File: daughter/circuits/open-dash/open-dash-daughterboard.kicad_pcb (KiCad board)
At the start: 4 copper layers, 125 x 100.1 mm, 220 parts, among them J1 Conn_01x01_Female, J10 Barrel_Jack_OD5.5_ID2.5, J11 Barrel_Jack_OD5.5_ID2.5, J12 AudioJack_3.5TRS, J13 AudioJack_3.5TRS, J14 Conn_02x03_Odd_Even, J15 USB_MINI_B, J16 Conn_02x02_Counter_Clockwise, J2 Conn_01x01_Female, J3 Conn_01x01_Female, J4 Conn_01x01_Female, J42 Conn_02x02_Counter_Clockwise, J43 Conn_02x02_Counter_Clockwise, J5 Conn_02x06_Odd_Even, J6 Conn_IDE_40, J7 Conn_IDE_40, J8 Conn_IDE_40, J9 Barrel_Jack_OD5.5_ID2.5, Q1 Crystal_12Mhz, Q10 Q_NPN_BEC, Q11 Q_AO3401A, Q12 Q_NPN_BEC, Q13 Q_NPN_BEC, Q14 Q_AO3400A, Q15 Q_NPN_BEC, Q16 Q_NPN_BEC, Q17 Q_AO3401A, Q18 Q_NPN_BEC, Q19 Q_NPN_BEC, Q2 Q_SS8050, Q20 Q_AO3400A, Q21 Q_NPN_BEC, Q22 Q_NPN_BEC, Q23 Q_AO3401A, Q24 Q_AO3400A, Q25 Q_AO3401A, Q26 Q_AO3400A, Q27 Q_AO3401A, Q28 Q_AO3400A, Q29 Q_AO3401A, Q3 Q_NPN_BEC, Q30 Q_AO3400A, Q31 Q_AO3401A, Q32 Q_AO3400A, Q33 Q_AO3401A, Q34 Q_AO3400A, Q35 Q_AO3401A, Q36 Q_AO3400A, Q37 Q_AO3401A, Q38 Q_AO3400A, Q39 Q_SS8550, Q4 Q_NPN_BEC, Q40 Q_AO3401A, Q5 Q_NPN_BEC, Q6 Q_NPN_BEC, Q7 Q_NPN_BEC, Q8 Q_NPN_BEC, Q9 Q_NPN_BEC, T1 Audio_Transformer, T2 Audio_Transformer, T3 Audio_Transformer, T4 Audio_Transformer, U1 Opto_TLP521, U10 Temp_Hum_HDC1080DMBR, U11 REG_AMS1117-3.3, U12 CH340T(SSOP20W), U13 MCP23017_SS, U14 ADC_ADS1015, U15 ADC_ADS1015, U16 ADC_ADS1015, U2 ACS711, U3 CAN_MCP2551-I-SN, U4 MIC29302WU, U5 MIC29302WU, U6 MIC29302WU, U7 TDA7851F, U8 Opto_TLP521, U9 ESP32-WROOM-32

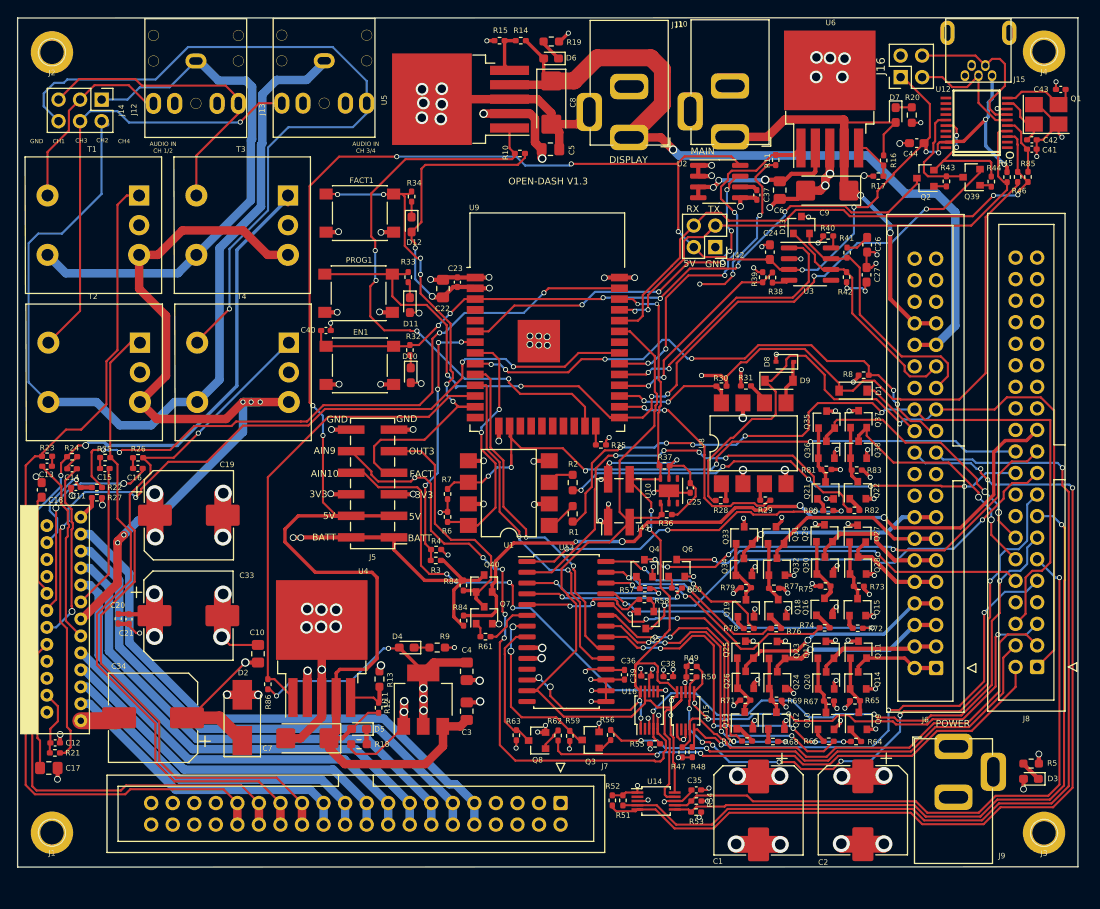
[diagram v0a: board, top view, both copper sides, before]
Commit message: send v1.4 to board house. Corrected source-drain on fets.
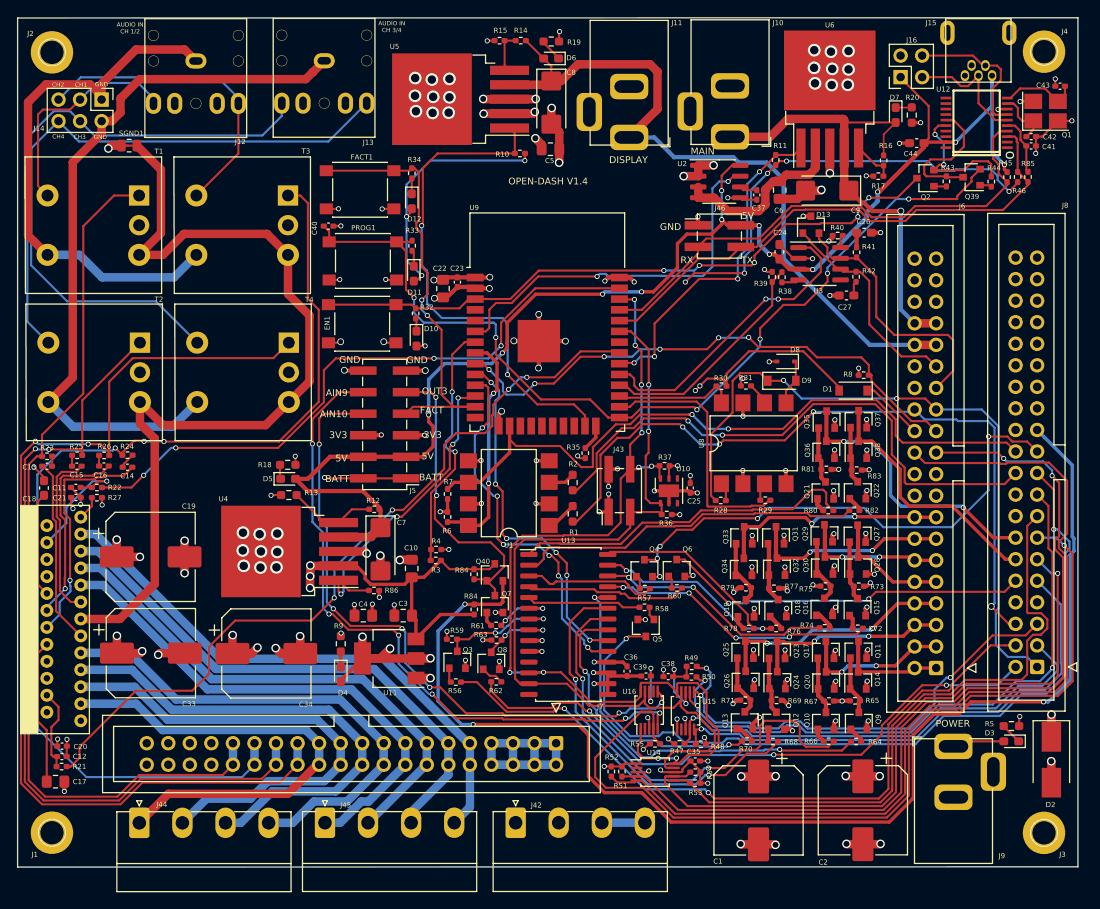
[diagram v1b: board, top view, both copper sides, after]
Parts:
- added J44: Terminal_01x04, Open_Automation:Terminal_1,5_4-G-5.08_1x04_P5.08mm_Horizontal, F.Cu at (102.5, 135.7)
- added J45: Terminal_01x04, Open_Automation:Terminal_1,5_4-G-5.08_1x04_P5.08mm_Horizontal, F.Cu at (124.4, 135.7)
- added J46: Conn_02x02_Counter_Clockwise, Connector_PinHeader_2.54mm:PinHeader_2x02_P2.54mm_Vertical_SMD, F.Cu at (170.9, 66.5)
- added SGND1: SGND_CONN, Open_Automation:SGND_CONN, F.Cu at (101.3, 55.9)
- D1, D9: value D_1N5819HW -> D_B5819W
- J42: value Conn_02x02_Counter_Clockwise -> Terminal_01x04; footprint Connector_PinHeader_2.54mm:PinHeader_2x02_P2.54mm_Vertical -> Open_Automation:Terminal_1,5_4-G-5.08_1x04_P5.08mm_Horizontal
- moved D2 95.5 mm to (210.0, 128.3), turned to 270 degrees
- moved J42 71.8 mm to (146.9, 135.7), turned to 0 degrees
- moved R18 34.0 mm to (120.0, 93.5), turned to 0 degrees
- moved D5 30.7 mm to (120.0, 95.2), turned to 0 degrees
- moved R13 24.2 mm to (120.1, 97.1), turned to 180 degrees
- moved C7 23.9 mm to (130.9, 103.5), turned to 270 degrees
- moved R12 23.4 mm to (130.2, 98.8), turned to 180 degrees
- moved C10 20.7 mm to (134.6, 105.7)
- moved R56 19.3 mm to (139.8, 119.1), turned to 180 degrees
- moved Q3 18.3 mm to (140.0, 116.5), turned to 90 degrees
- moved R59 18.0 mm to (139.3, 114.1), turned to 180 degrees
- moved R86 16.7 mm to (130.2, 108.3), turned to 0 degrees
- moved C20 16.4 mm to (93.4, 126.7), turned to 180 degrees
- moved C21 15.6 mm to (95.0, 97.3), turned to 0 degrees
- moved C34 15.4 mm to (117.5, 115.8), turned to 0 degrees
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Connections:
- C3 pad 1: /5V -> /BATTERY
- C40 pad 1: /ESP_EN -> /PROG
- J42 pad 2: /5V -> GND
- J42 pad 3: /TXD -> /BATTERY
- J42 pad 4: /RXD -> /BATTERY
- Q11 pad 2: /LEFT_AIR_TEMP_CONTROL_A -> /BATTERY
- Q11 pad 3: /BATTERY -> /LEFT_AIR_TEMP_CONTROL_A
- Q17 pad 2: /LEFT_AIR_TEMP_CONTROL_B -> /BATTERY
- Q17 pad 3: /BATTERY -> /LEFT_AIR_TEMP_CONTROL_B
- Q23 pad 2: /RIGHT_AIR_TEMP_CONTROL_A -> /BATTERY
- Q23 pad 3: /BATTERY -> /RIGHT_AIR_TEMP_CONTROL_A
- Q25 pad 2: /RIGHT_AIR_TEMP_CONTROL_B -> /BATTERY
- Q25 pad 3: /BATTERY -> /RIGHT_AIR_TEMP_CONTROL_B
- Q27 pad 2: /MODE_A -> /BATTERY
- Q27 pad 3: /BATTERY -> /MODE_A
- Q29 pad 2: /MODE_B -> /BATTERY
- Q29 pad 3: /BATTERY -> /MODE_B
- Q31 pad 2: /RECIRCULATION_A -> /BATTERY
- Q31 pad 3: /BATTERY -> /RECIRCULATION_A
- Q33 pad 2: /RECIRCULATION_B -> /BATTERY
- Q33 pad 3: /BATTERY -> /RECIRCULATION_B
- Q35 pad 2: /DRIVER_SEAT_TEMP_CONTROL -> /BATTERY
- Q35 pad 3: /BATTERY -> /DRIVER_SEAT_TEMP_CONTROL
- Q37 pad 2: /PASSENGER_SEAT_TEMP_CONTROL -> /BATTERY
- Q37 pad 3: /BATTERY -> /PASSENGER_SEAT_TEMP_CONTROL
- U11 pad 3: /5V -> /BATTERY
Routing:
- net /5V: track 258.2 -> 168.9 mm, vias 11 -> 12
- net GND: track 296.1 -> 228.2 mm, vias 132 -> 145
- net /EXT_AMP_ON: track 86.3 -> 145.9 mm, vias 4 -> 3
- net /REAR_DEFOG: track 55.2 -> 98.0 mm
- net /PASSENGER_SUNLOAD: track 70.1 -> 104.7 mm, vias 3 -> 1
- net /AUDIO_IN4: track 86.2 -> 120.5 mm, vias 1 -> 2
- net /3V3: track 218.7 -> 186.7 mm, vias 34 -> 40
- net /BATTERY: track 124.0 -> 151.0 mm, vias 38 -> 42
- net /DRIVER_HEATED_SEAT_STATUS: track 57.3 -> 83.6 mm
- net /Audio Amplifier/AUDIO_GND2: track 108.9 -> 85.8 mm
- net /AIN10: track 55.4 -> 76.8 mm, vias 4 -> 6
- net /RF-: track 36.0 -> 56.6 mm
- net /AUDIO_IN3: track 76.4 -> 96.7 mm, vias 0 -> 2
- net /5V_EN: track 56.1 -> 37.3 mm, vias 0 -> 4
- net /RF+: track 39.4 -> 57.4 mm
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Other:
- board text added: "OPEN-DASH V1.4"
- board text removed: "OPEN-DASH V1.3"

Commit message: updated schematic
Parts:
- added C28: C_47uF, Capacitor_SMD:C_1210_3225Metric_Pad1.33x2.70mm_HandSolder, F.Cu at (91.7, 128.0)
- C17: value C_10uF -> C_1uF; footprint Capacitor_SMD:C_0805_2012Metric_Pad1.18x1.45mm_HandSolder -> Capacitor_SMD:C_0402_1005Metric_Pad0.74x0.62mm_HandSolder
- moved C17 2.51 mm to (95.0, 130.0)
- moved R21 1.55 mm to (94.9, 128.8)
- moved C12 1.55 mm to (94.9, 127.6)
- moved C20 1.55 mm to (94.9, 126.4)
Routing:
- net GND: track 228.2 -> 229.5 mm, vias 145 -> 146
- net /Audio Amplifier/STBY: track 9.90 -> 9.31 mm

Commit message: Updated schematic
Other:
- net class Default removed
- net class HIGH CURRENT removed
- net class LOW CURRENT removed
- net class MED CURRENT removed
